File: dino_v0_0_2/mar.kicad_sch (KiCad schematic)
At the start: 10 parts, among them U54 74LS245, U55 74LS373, U58 74LS373, U59 74LS245, U60 74LS02

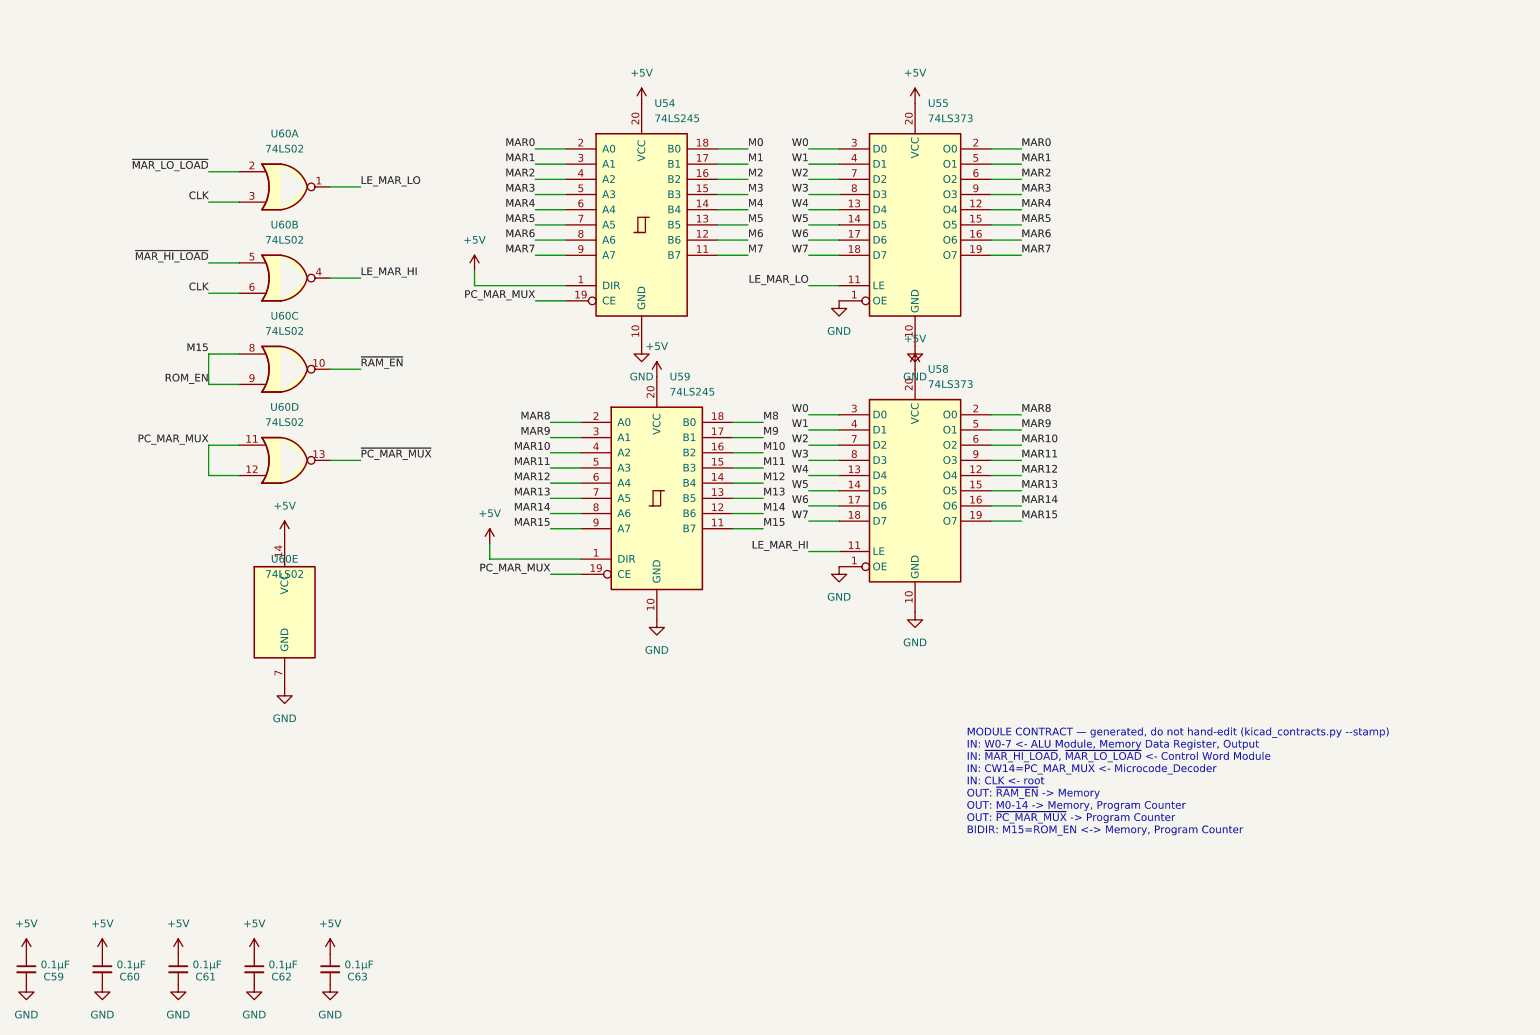
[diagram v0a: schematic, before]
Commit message: Machine Complete
All ten DINO modules bench-proven on the ATmega2560 rig: root, pc,
microcode, control_word, mdr, registers, mar, memory, alu, io. Coverage
lint reports 0 gaps and 0 pending.

Test modules (mod_*.c) plus host-tested expect models (cw/mdr/reg/mar/
mem/alu_expect.h) — pure logic, no AVR headers, exhaustive host tests
written RED before any bench run. Every assertion was netlist-verified
against the schematic before it was encoded.

Generators, so no table is hand-maintained:
  kicad_contracts.py   contracts + pinmap from the KiCad netlist
  microcode_gen.py     microcode ROM images
  progrom_gen.py       program ROM (DIAG + the milestone program)
  layout_gen.py        breadboard placement, slot maps, wiring guides

Two house rules learned the hard way and now codified in BRINGUP.md:
  mirror-witness   a write-then-read through one bus bank is
                   permutation-blind; every module needs an asymmetric
                   path (this is what caught the flipped PORTF->MDR bank)
  phantom power    rig lines feed DUT VCC through input clamp diodes, so
                   an unpowered board reads fine; every module gets a
                   power test holding outputs at the non-sourcing level

The ALU slot map in layout_gen.py is AS-BUILT and FROZEN — read off the
strip by beeping each slot to its chip pin, not derived. Once a strip is
populated its slot map is copper.

Housekeeping: .gitignore for __pycache__, KiCad .lck, Obsidian workspace
state, and compiled host-test binaries; those are untracked here.

Next: the integration ladder (INT-A/B/B2/C/D/E), then free-run of
LDAI 5; LDBI 3; ADD; OUT; HALT — the milestone, where the machine adds
two numbers.

Co-Authored-By: Claude Opus 5 (1M context) <noreply@anthropic.com>
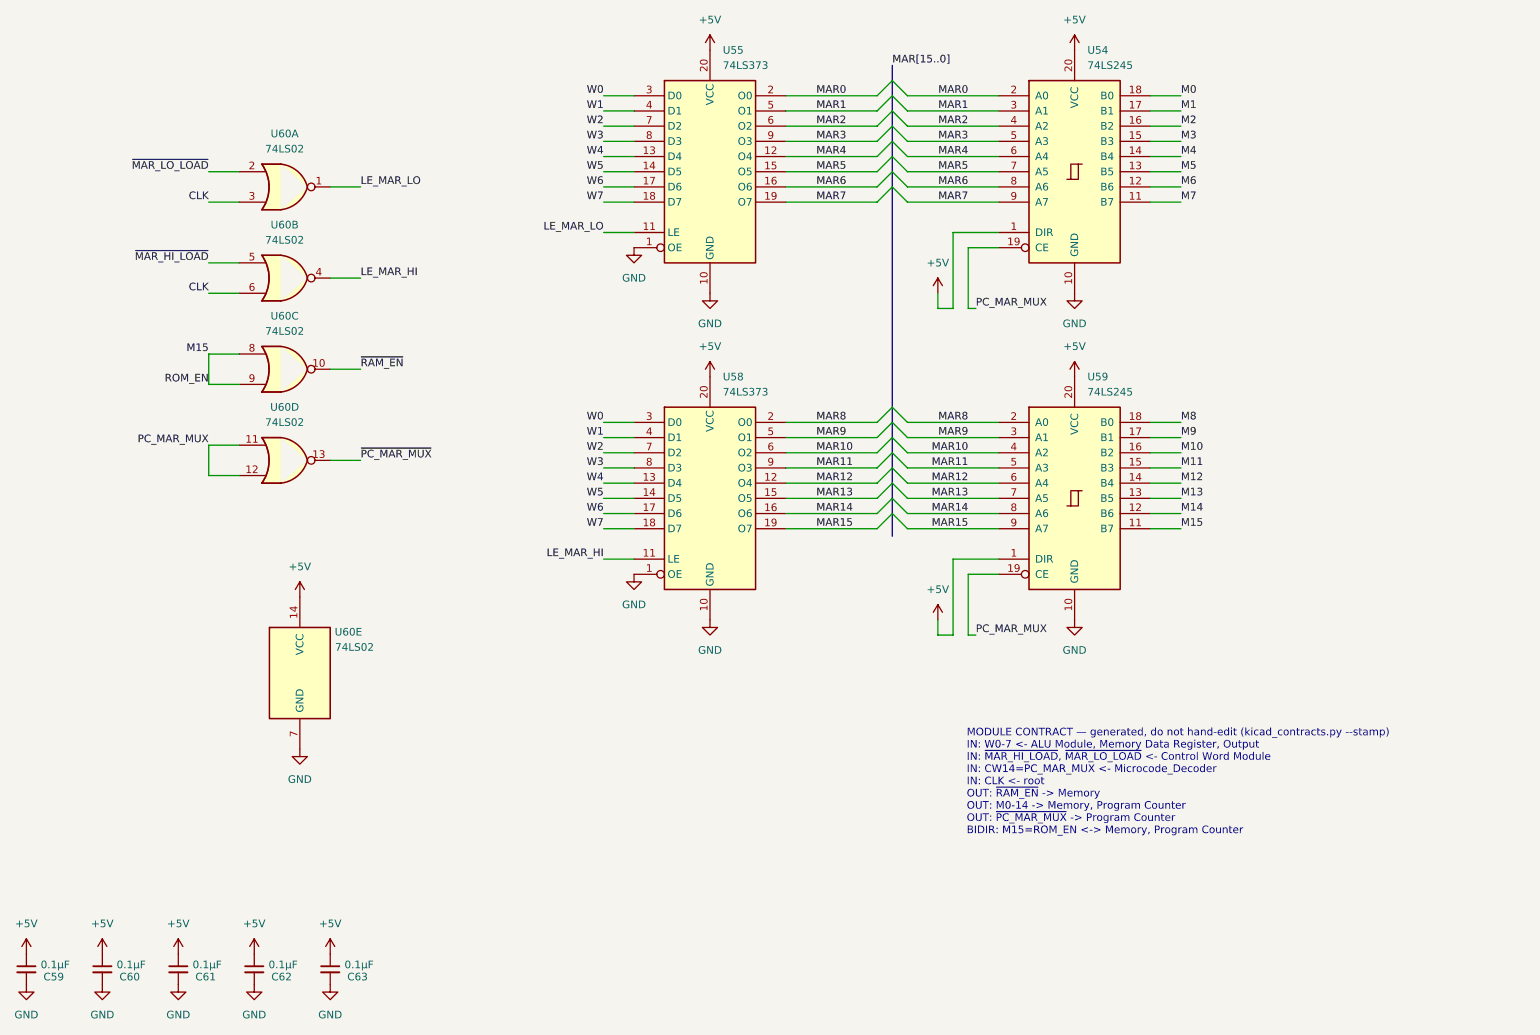
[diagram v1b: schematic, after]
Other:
- moved on the sheet: U54, U55, U58, U59, U60E

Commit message: schematic: join five aliased nets, and ledger the root-sheet gap
FIVE LIVE WIRES WERE IN THE CHECKLIST'S NO-CONNECT BUCKET, under the
heading "nothing to land and nothing to beep against."

  CW9/SA2           U15.12  <->  U38.7, U40.7
  CW10/SA1          U15.13  <->  U38.6, U40.6, U53.12
  CW11/SA0          U15.15  <->  U38.5, U40.5, U53.13
  CW13/PC_UP        U15.17  <->  U36.1
  CW14/PC_MAR_MUX   U15.18  <->  U54.19, U59.19, U60.11, U60.12

The microcode sheet labelled each net CWnn; the consumer sheet labelled it
SA2 / PC_UP / PC_MAR_MUX. Two label sets, two net keys, both look
sheet-local, and the cross-sheet filter drops the wire -- the M15/ROM_EN
failure, five more times.

alias_splits() could not see it. It keys on a shared BASE label, which is
how it catches CW17 vs CW17/~{SRC_BANK}. CW9 and SA2 share no substring,
so the guard was structurally blind to this shape.

Applied via kicad_gen_sheet.py ops files -- deterministic uuid5, applied
markers, valid s-expression splices -- not hand edits. Every touched sheet
reparses. dino_sheet_contracts.md is UNCHANGED, which confirms the
contracts path (hierarchical sheet pins) was always right and only the
checklist path was blind. unlanded_stubs 20 -> 14; the five now emit as
NEW: with beep partners.

Cosmetic: CW13 on program_counter sits at the same coordinate as PC_UP.
That anchor has no horizontal run, and same-point is the only placement
guaranteed to attach to the right node. Drag apart in KiCad when convenient.

A THIRD BLIND SPOT, FOUND AND LEDGERED RATHER THAN FIXED. net_pins()
walks the ten child sheets and NOT the root sheet:

    alu control_word input_output mar mdr memory microcode
    program_counter registers_a_b stack_pointer      -- no root

Root carries U6 (T-counter), U7/U8 (T decoders), U20 (divider), U27
(clock/reset), U56, U61, Y1, SW2 -- real parts on no child sheet. Their
pins can never reach a continuity checklist, and any child-sheet net
terminating on root is misreported as a no-connect. 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
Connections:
- net PC_MAR_MUX renamed CW14
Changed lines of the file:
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@@
+		)
+	)
+	(label "CW14"
+		(at 53.34 99.06 0)
+		(effects
+			(font
+				(size 1.27 1.27)
+			)
+			(justify left bottom)
 		)
 	)

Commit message: feat: phase D on silicon — the machine executes from RAM
PROG_ramexec returns 0x6E. The PC has been above 0x7FFF and FETCH_RAM has
been high, both for the first time in this machine's life.

The missing condition was never "is this a fetch." ~ROM_OUT is asserted for
every src=ROM — opcode fetch, LDAI's immediate, LDA/STA/JMP/CALL operand
bytes — so an instruction living in RAM must read its operands from RAM
too. The condition is "a ROM-side read was requested, but the address is
above 0x7FFF":

    FETCH_RAM = NOR(~ROM_OUT, ~RAM_EN)

Six gate sections, no new IC. All six were free on U22/U37/U39, already in
sockets on the MDR board, where ~ROM_OUT and ~RAM_OUT already sit feeding
READS_IDLE. Only ~RAM_EN had to be brought in.

    U22 g3   FETCH_RAM     = NOR(~ROM_OUT, ~RAM_EN)
    U22 g4   ROM_BUF_ON    = NOR(~ROM_OUT, FETCH_RAM)
    U37 inv4 ~{FETCH_RAM}
    U37 inv6 ~{ROM_BUF_EN} = OR(~ROM_OUT, FETCH_RAM)   -> U19.19
    U37 inv5 ~{RAM_OE_G}   = AND(~RAM_OUT, ~FETCH_RAM) -> U26.22 + U51.9
    U39 g4   RAM_OE_ON     = NAND(~RAM_OUT, ~FETCH_RAM)

Two pin lifts on the memory board, eleven wires. U24.22 stays on ~ROM_OUT:
U24's own ~CE = M15 already deselects the ROM chip at RAM addresses.

Gating ~RAM_OUT upstream is what keeps this at six gates rather than eight.
U51 is a 7400 computing ~RAM_MDR_EN = AND(~RAM_OUT, ~WRITE_DIR), so one
gate on ~RAM_OUT moves both the RAM chip's ~OE and its buffer's ~CE.

Re-proved before building: all 15 src=ROM microcode rows carry mux_pc=True,
FETCH included, and FILL is src=NONE. A ROM-side read can now land in RAM,
so the standing "ROM reads are exempt from the src=RAM -> MAR loop" rule was
no longer free. It holds — MAR never drives M during a ROM-side read, and a
runaway opcode cannot open the loop either.

The witness is not permutation-blind. If the fetch had still come from ROM,
PC=0x9000 presents A0-A14 = 0x1000 to U24, which is 0xFF fill, which is
HALT, so the poison would have survived as 0xFF. 0x6E is 0x8B - 0x1D,
compu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
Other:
- note added: "MODULE CONTRACT — generated, do not hand-edit (kicad_contracts.py --stamp) IN: W0-7 <- ALU Module, Memory Data Register, Output IN: ~{MAR_HI_LOAD}, ~{MAR_LO_LOAD} <- Control Word Module IN: CW14=PC_MAR_MUX <- Microcode_Decoder IN: CLK <- root OUT: ~{RAM_EN} -> Memory, Memory Data Register OUT: M0-14 -> Memory, Program Counter OUT: ~{PC_MAR_MUX} -> Program Counter BIDIR: M15=ROM_EN <-> Memory, Pro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"
- note removed: "MODULE CONTRACT — generated, do not hand-edit (kicad_contracts.py --stamp) IN: W0-7 <- ALU Module, Memory Data Register, Output IN: ~{MAR_HI_LOAD}, ~{MAR_LO_LOAD} <- Control Word Module IN: CW14=PC_MAR_MUX <- Microcode_Decoder IN: CLK <- root OUT: ~{RAM_EN} -> Memory OUT: M0-14 -> Memory, Program Counter OUT: ~{PC_MAR_MUX} -> Program Counter BIDIR: M15=ROM_EN <-> Memory, Program Counter"
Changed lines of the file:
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@@
 		(comment 4 "A Turing-Complete 8-bit \"Computer\"")
 	)
-	(text "MODULE CONTRACT — generated, do not hand-edit (kicad_contracts.py --stamp)\nIN: W0-7 <- ALU Module, Memory Data Register, Output\nIN: ~{MAR_HI_LOAD}, ~{MAR_LO_LOAD} <- Control Word Module\nIN: CW14=PC_MAR_MUX <- Microcode_Decoder\nIN: CLK <- root\nOUT: ~{RAM_EN} -> Memory\nOUT: M0-14 -> Memory, Program Counter\nOUT: ~{PC_MAR_MUX} -> Program Counter\nBIDIR: M15=ROM_EN <-> Memory, Program Counter"
-		(exclude_from_sim no)
-		(at 177.546 164.338 0)
-		(effects
-			(font
-				(size 1.27 1.27)
-			)
-			(justify left bottom)
-		)
-	)
 	(bus_entry
 		(at 165.1 53.34)
@@
 		)
 	)
+	(text "MODULE CONTRACT — generated, do not hand-edit (kicad_contracts.py --stamp)\nIN: W0-7 <- ALU Module, Memory Data Register, Output\nIN: ~{MAR_HI_LOAD}, ~{MAR_LO_LOAD} <- Control Word Module\nIN: CW14=PC_MAR_MUX <- Microcode_Decoder\nIN: CLK <- root\nOUT: ~{RAM_EN} -> Memory, Memory Data Register\nOUT: M0-14 -> Memory, Program Counter\nOUT: ~{PC_MAR_MUX} -> Program Counter\nBIDIR: M15=ROM_EN <-> Memory, Program Counter"
+		(exclude_from_sim no)
+		(at 177.546 164.338 0)
+		(effects
+			(font
+				(size 1.27 1.27)
+			)
+			(justify left bottom)
+		)
+	)

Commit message: feat: phase E step A -- the 16K I/O window, in schematic
Carves 0x4000-0x7FFF out of ROM space and publishes a bus. The ROM now
answers 0x0000-0x3FFF only; the window decodes to no core chip, so W
reads its park -- 0xFF, which is HALT.

TWO NEW PACKAGES, both on the memory board:

  U74 '00  ~{M14}      = NAND(M14, M14)
           ~{ROM_SEL}  = NAND(~{RAM_EN}, ~{M14})
           ~{RAM_OE_G} = NAND(RAM_OE_ON, M15)
           ~{IO_SEL}   = NAND(~{RAM_EN}, M14)
  U75 '32  ~{IO_RD}    = OR(~{IO_SEL}, READS_IDLE)
           ~{IO_WR}    = OR(~{IO_SEL}, ~{RAM_WRITE_EN})
           RESET_B     = OR(RESET, GND)
           ~{IO_RD_Q}  = OR(~{IO_RD}, CLK)

Eight copper changes: U24.20 and U22.12 to ~{ROM_SEL}, U26.22/U51.9 fed
from U74 g3, U39.10 to ~{IO_RD}, U37.10 and U28.7 unlanded, U37.11 to
GND. Park: R4-R8 + R25-R27, 4.7k on W0-7. CLK crosses through R3, 100R,
source end -- the R2 treatment.

IN RETIRES. ~{SW_OUT} has zero pins project-wide. SWITCH-GATE1's enables
are strapped +5V until card zero drives them from an address decode.

THE ROM_EN ALIAS IS DELETED. Once U24.20 moved, ROM_EN named a net with
no ROM consumer. Deleting it half-way SPLIT the net and alias_splits()
caught it mid-edit -- M15: ['M15', 'M15/ROM_EN'], the exact two-key
failure that once cost this project the ROM chip-enable on every
continuity checklist ever generated.

CLK WAS A FOURTH CROSSING THE SPEC DID NOT CARRY. Census: 15 CLK pins,
none on the memory board; ~{CLK} at U51.4 is the wrong polarity and both
new packages are full. SECTION 1's cost table predated the read-term
split that spent U75 g4, so memory is +4 and MDR is +4 -- the wire margin
is zero. Ruled: stay on memory, the output-load argument still holds.

SWITCH-GATE1/SW1/R17-R24/C48 move to their own input.kicad_sch so the
DIP card is modelled as a card. No renumbering: 168 designators
unchanged, --since reports annotate=0.

TOOLING RECONCILED TO THE DESIGN, not the reverse:
  test_continuity_completeness  M15_PINS U24.20 -> U74.10; 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
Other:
- note added: "MODULE CONTRACT — generated, do not hand-edit (kicad_contracts.py --stamp) IN: W0-7 <- ALU Module, Input, Memory Data Register IN: ~{MAR_HI_LOAD}, ~{MAR_LO_LOAD} <- Control Word Module IN: CW14=PC_MAR_MUX <- Microcode_Decoder IN: CLK <- root OUT: ~{RAM_EN} -> Memory, Memory Data Register OUT: M0-14 -> Memory, Program Counter OUT: ~{PC_MAR_MUX} -> Program Counter BIDIR: M15 <-> Memory, Program Cou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"
- note removed: "MODULE CONTRACT — generated, do not hand-edit (kicad_contracts.py --stamp) IN: W0-7 <- ALU Module, Memory Data Register, Output IN: ~{MAR_HI_LOAD}, ~{MAR_LO_LOAD} <- Control Word Module IN: CW14=PC_MAR_MUX <- Microcode_Decoder IN: CLK <- root OUT: ~{RAM_EN} -> Memory, Memory Data Register OUT: M0-14 -> Memory, Program Counter OUT: ~{PC_MAR_MUX} -> Program Counter BIDIR: M15=ROM_EN <-> Memory, Pro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"
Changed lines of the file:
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@@
 		)
 	)
-	(label "ROM_EN"
-		(at 50.8 88.9 180)
-		(effects
-			(font
-				(size 1.27 1.27)
-			)
-			(justify right bottom)
-		)
-	)
 	(label "MAR2"
 		(at 152.4 45.72 0)
@@
 		)
 	)
-	(text "MODULE CONTRACT — generated, do not hand-edit (kicad_contracts.py --stamp)\nIN: W0-7 <- ALU Module, Memory Data Register, Output\nIN: ~{MAR_HI_LOAD}, ~{MAR_LO_LOAD} <- Control Word Module\nIN: CW14=PC_MAR_MUX <- Microcode_Decoder\nIN: CLK <- root\nOUT: ~{RAM_EN} -> Memory, Memory Data Register\nOUT: M0-14 -> Memory, Program Counter\nOUT: ~{PC_MAR_MUX} -> Program Counter\nBIDIR: M15=ROM_EN <-> Memory, Program Counter"
+	(text "MODULE CONTRACT — generated, do not hand-edit (kicad_contracts.py --stamp)\nIN: W0-7 <- ALU Module, Input, Memory Data Register\nIN: ~{MAR_HI_LOAD}, ~{MAR_LO_LOAD} <- Control Word Module\nIN: CW14=PC_MAR_MUX <- Microcode_Decoder\nIN: CLK <- root\nOUT: ~{RAM_EN} -> Memory, Memory Data Register\nOUT: M0-14 -> Memory, Program Counter\nOUT: ~{PC_MAR_MUX} -> Program Counter\nBIDIR: M15 <-> Memory, Program Counter"
 		(exclude_from_sim no)
 		(at 177.546 164.338 0)
